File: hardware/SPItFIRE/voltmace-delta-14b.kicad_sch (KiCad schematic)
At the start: 17 parts, among them J2 DA15_Pins, SW10 SW_Push_45deg, SW10L1 SW_Push_45deg, SW10M1 SW_Push_45deg, SW10R1 SW_Push_45deg, SW12 SW_Push_45deg, SW13 SW_Push_45deg, SW14 SW_Push_45deg, SW15 SW_Push_45deg, SW16 SW_Push_45deg, SW17 SW_Push_45deg, SW18 SW_Push_45deg, SW19 SW_Push_45deg, SW20 SW_Push_45deg, SW21 SW_Push_45deg

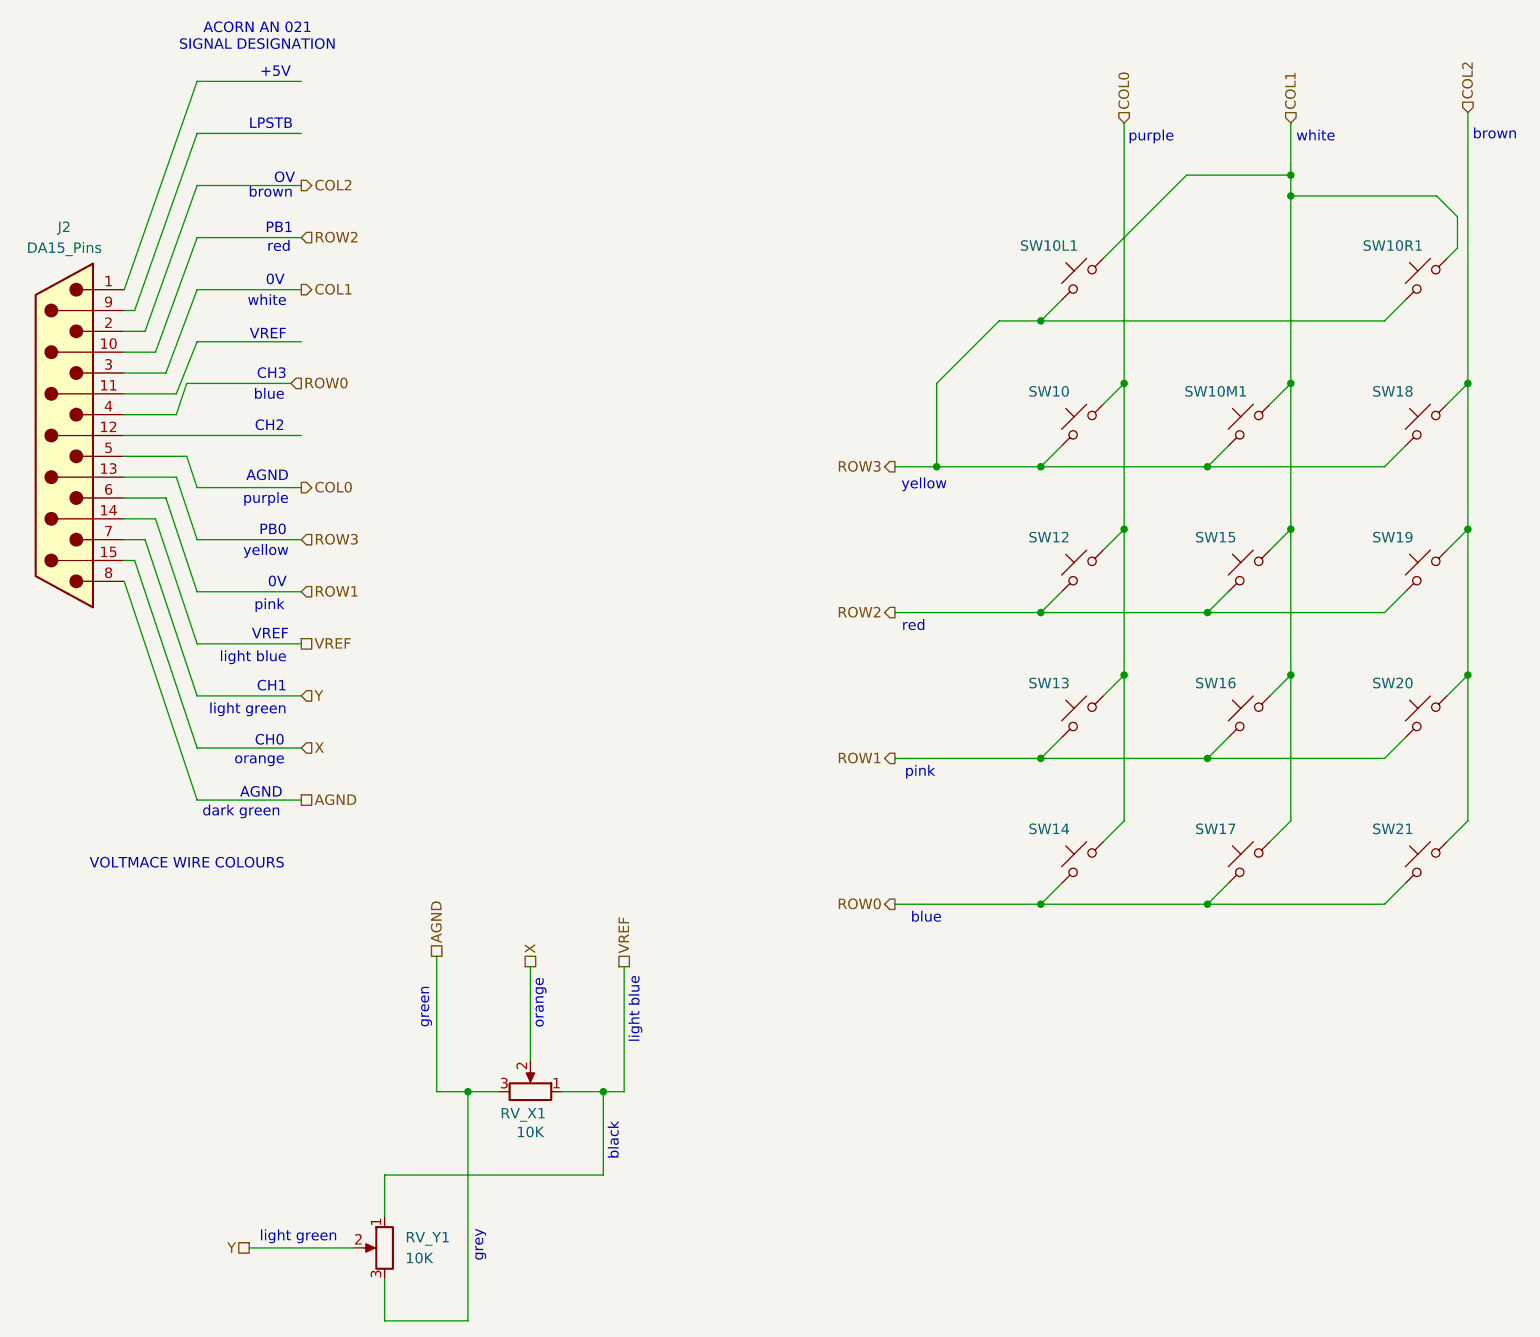
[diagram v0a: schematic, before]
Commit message: Voltmace pinouts
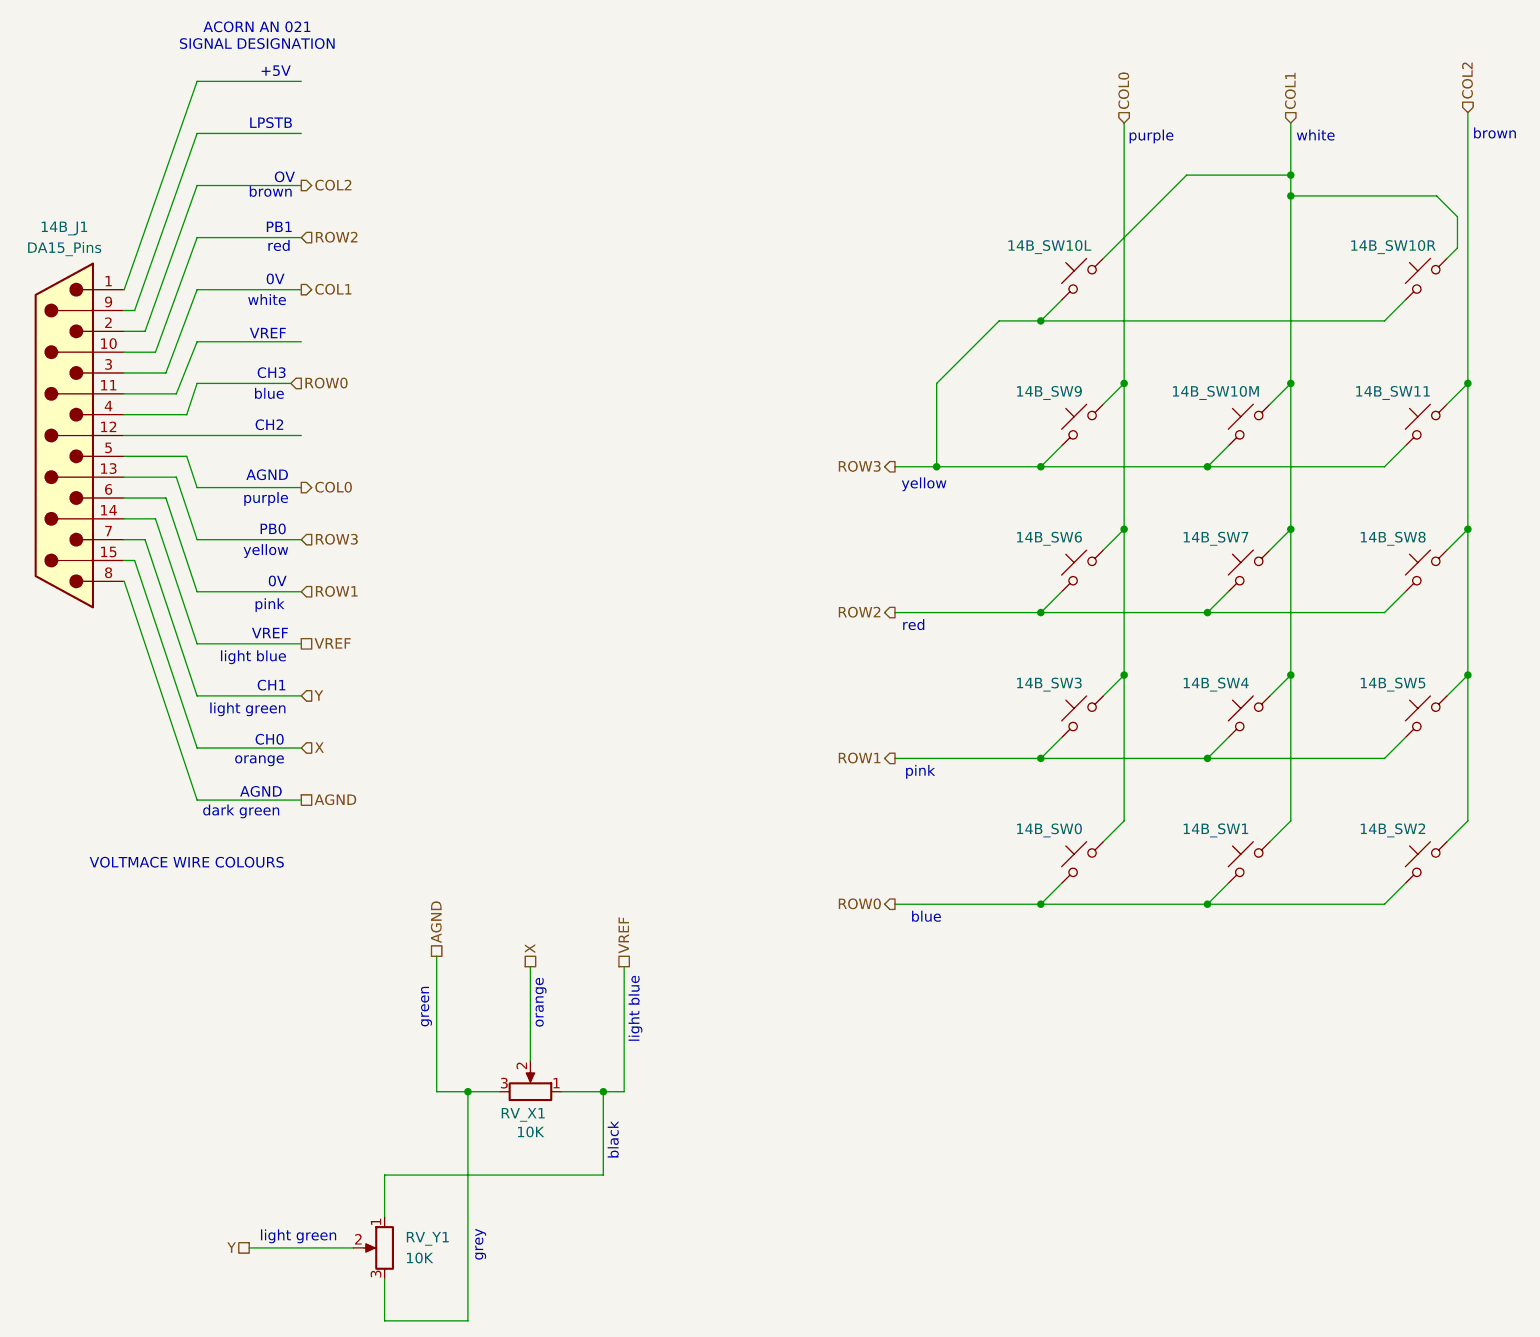
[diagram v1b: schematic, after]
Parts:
- renumbered J2 to 14B_J1, SW14 to 14B_SW0, SW17 to 14B_SW1, SW10L1 to 14B_SW10L, SW10M1 to 14B_SW10M, SW10R1 to 14B_SW10R, SW18 to 14B_SW11, SW21 to 14B_SW2, SW13 to 14B_SW3, SW16 to 14B_SW4, SW20 to 14B_SW5, SW12 to 14B_SW6, SW15 to 14B_SW7, SW19 to 14B_SW8, SW10 to 14B_SW9
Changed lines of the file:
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@@
 	(wire
 		(pts
-			(xy 71.12 69.85) (xy 72.39 66.04)
+			(xy 72.39 69.85) (xy 73.66 66.04)
 		)
 		(stroke
@@
 	(wire
 		(pts
-			(xy 72.39 66.04) (xy 85.09 66.04)
+			(xy 73.66 66.04) (xy 85.09 66.04)
 		)
 		(stroke
@@
 	(wire
 		(pts
-			(xy 64.77 69.85) (xy 71.12 69.85)
+			(xy 64.77 69.85) (xy 72.39 69.85)
 		)
 		(stroke
@@
 		(on_board yes)
 		(dnp no)
-		(property "Reference" "SW20"
+		(property "Reference" "14B_SW5"
 			(at 219.456 102.616 0)
 			(effects
@@
 			(project "SPItFIRE"
 				(path "/148e0ceb-efca-48fe-9d35-9803ba402dc8/b2803d4d-10bd-4088-a3d9-c185506ad2c5"
-					(reference "SW20")
+					(reference "14B_SW5")
 					(unit 1)
 				)
@@
 		(on_board yes)
 		(dnp no)
-		(property "Reference" "SW10L1"
+		(property "Reference" "14B_SW10L"
 			(at 177.546 49.276 0)
 			(effects
@@
 			(project "SPItFIRE"
 				(path "/148e0ceb-efca-48fe-9d35-9803ba402dc8/b2803d4d-10bd-4088-a3d9-c185506ad2c5"
-					(reference "SW10L1")
+					(reference "14B_SW10L")
 					(unit 1)
 				)
@@
 		(on_board yes)
 		(dnp no)
-		(property "Reference" "SW13"
+		(property "Reference" "14B_SW3"
 			(at 177.546 102.616 0)
 			(effects
@@
 			(project "SPItFIRE"
 				(path "/148e0ceb-efca-48fe-9d35-9803ba402dc8/b2803d4d-10bd-4088-a3d9-c185506ad2c5"
-					(reference "SW13")
+					(reference "14B_SW3")
 					(unit 1)
 				)
@@
 		(on_board yes)
 		(dnp no)
-		(property "Reference" "SW21"
+		(property "Reference" "14B_SW2"
 			(at 219.456 120.396 0)
 			(effects
@@
 			(project "SPItFIRE"
 				(path "/148e0ceb-efca-48fe-9d35-9803ba402dc8/b2803d4d-10bd-4088-a3d9-c185506ad2c5"
-					(reference "SW21")
+					(reference "14B_SW2")
 					(unit 1)
 				)
@@
 		(on_board yes)
 		(dnp no)
-		(property "Reference" "SW12"
+		(property "Reference" "14B_SW6"
 			(at 177.546 84.836 0)
 			(effects
@@
 			(project "SPItFIRE"
 				(path "/148e0ceb-efca-48fe-9d35-9803ba402dc8/b2803d4d-10bd-4088-a3d9-c185506ad2c5"
-					(reference "SW12")
+					(reference "14B_SW6")
 					(unit 1)
 				)
@@
 		(on_board yes)
 		(dnp no)
-		(property "Reference" "SW18"
+		(property "Reference" "14B_SW11"
 			(at 219.456 67.056 0)
 			(effects
@@
 			(project "SPItFIRE"
 				(path "/148e0ceb-efca-48fe-9d35-9803ba402dc8/b2803d4d-10bd-4088-a3d9-c185506ad2c5"
-					(reference "SW18")
+					(reference "14B_SW11")
 					(unit 1)
 				)
@@
 		(on_board yes)
 		(dnp no)
-		(property "Reference" "SW10M1"
+		(property "Reference" "14B_SW10M"
 			(at 197.866 67.056 0)
 			(effects
@@
 			(project "SPItFIRE"
 				(path "/148e0ceb-efca-48fe-9d35-9803ba402dc8/b2803d4d-10bd-4088-a3d9-c185506ad2c5"
-					(reference "SW10M1")
+					(reference "14B_SW10M")
 					(unit 1)
 				)
@@
 		(on_board yes)
 		(dnp no)
-		(property "Reference" "SW10"
+		(property "Reference" "14B_SW9"
 			(at 177.546 67.056 0)
 			(effects
@@
 			(project "SPItFIRE"
 				(path "/148e0ceb-efca-48fe-9d35-9803ba402dc8/b2803d4d-10bd-4088-a3d9-c185506ad2c5"
-					(reference "SW10")
+					(reference "14B_SW9")
 					(unit 1)
 				)
@@
 		(on_board yes)
 		(dnp no)
-		(property "Reference" "SW10R1"
+		(property "Reference" "14B_SW10R"
 			(at 219.456 49.276 0)
 			(effects
@@
 			(project "SPItFIRE"
 				(path "/148e0ceb-efca-48fe-9d35-9803ba402dc8/b2803d4d-10bd-4088-a3d9-c185506ad2c5"
-					(reference "SW10R1")
+					(reference "14B_SW10R")
 					(unit 1)
 				)
@@
 		(on_board yes)
 		(dnp no)
-		(property "Reference" "SW14"
+		(property "Reference" "14B_SW0"
 			(at 177.546 120.396 0)
 			(effects
@@
 			(project "SPItFIRE"
 				(path "/148e0ceb-efca-48fe-9d35-9803ba402dc8/b2803d4d-10bd-4088-a3d9-c185506ad2c5"
-					(reference "SW14")
+					(reference "14B_SW0")
 					(unit 1)
 				)
@@
 		(on_board yes)
 		(dnp no)
-		(property "Reference" "SW17"
+		(property "Reference" "14B_SW1"
 			(at 197.866 120.396 0)
 			(effects
@@
 			(project "SPItFIRE"
 				(path "/148e0ceb-efca-48fe-9d35-9803ba402dc8/b2803d4d-10bd-4088-a3d9-c185506ad2c5"
-					(reference "SW17")
+					(reference "14B_SW1")
 					(unit 1)
 				)
@@
 		(on_board yes)
 		(dnp no)
-		(property "Reference" "SW15"
+		(property "Reference" "14B_SW7"
 			(at 197.866 84.836 0)
 			(effects
@@
 			(project "SPItFIRE"
 				(path "/148e0ceb-efca-48fe-9d35-9803ba402dc8/b2803d4d-10bd-4088-a3d9-c185506ad2c5"
-					(reference "SW15")
+					(reference "14B_SW7")
 					(unit 1)
 				)
@@
 		(on_board yes)
 		(dnp no)
-		(property "Reference" "SW19"
+		(property "Reference" "14B_SW8"
 			(at 219.456 84.836 0)
 			(effects
@@
 			(project "SPItFIRE"
 				(path "/148e0ceb-efca-48fe-9d35-9803ba402dc8/b2803d4d-10bd-4088-a3d9-c185506ad2c5"
-					(reference "SW19")
+					(reference "14B_SW8")
 					(unit 1)
 				)
@@
 		(dnp no)
 		(fields_autoplaced yes)
-		(property "Reference" "J2"
+		(property "Reference" "14B_J1"
 			(at 57.4675 46.99 0)
 			(effects
@@
 			(project "SPItFIRE"
 				(path "/148e0ceb-efca-48fe-9d35-9803ba402dc8/b2803d4d-10bd-4088-a3d9-c185506ad2c5"
-					(reference "J2")
+					(reference "14B_J1")
 					(unit 1)
 				)
@@
 		(on_board yes)
 		(dnp no)
-		(property "Reference" "SW16"
+		(property "Reference" "14B_SW4"
 			(at 197.866 102.616 0)
 			(effects
@@
 			(project "SPItFIRE"
 				(path "/148e0ceb-efca-48fe-9d35-9803ba402dc8/b2803d4d-10bd-4088-a3d9-c185506ad2c5"
-					(reference "SW16")
+					(reference "14B_SW4")
 					(unit 1)
 				)

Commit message: Update schematic naming convention to keep Kicad happy
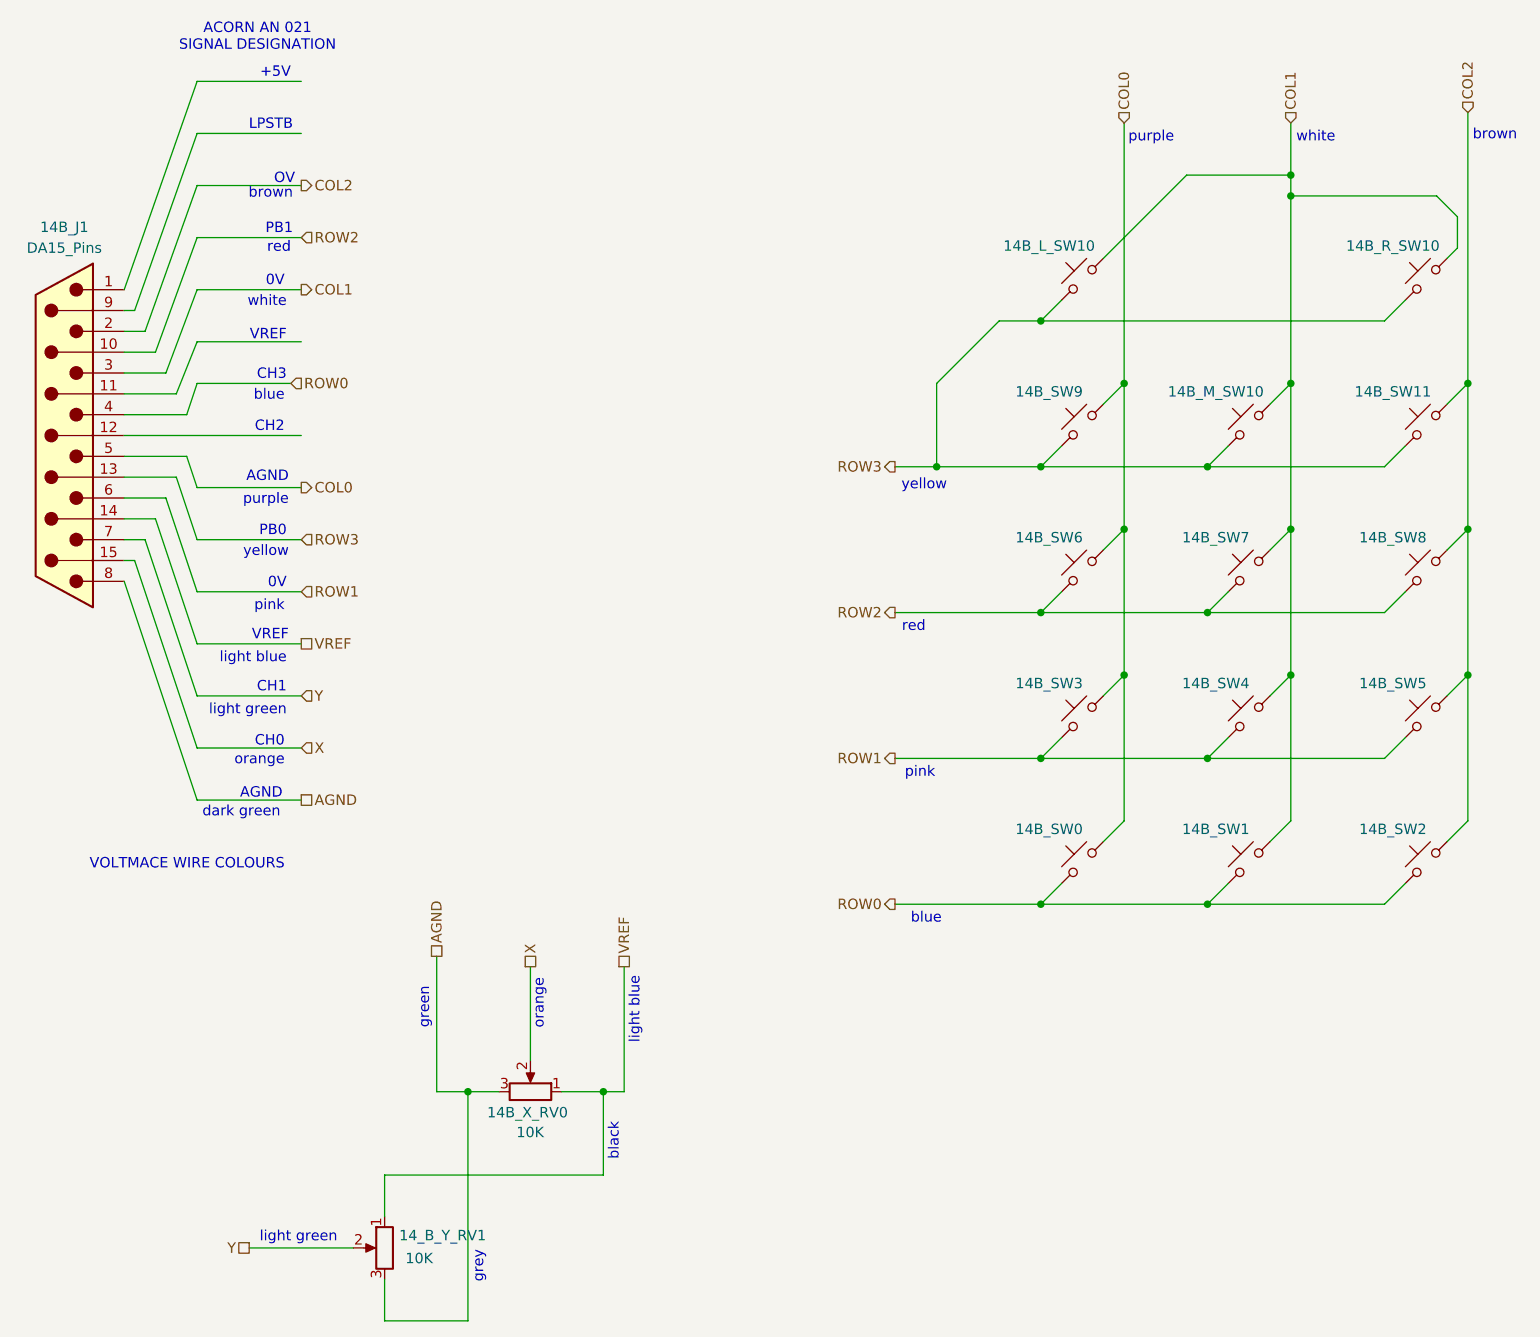
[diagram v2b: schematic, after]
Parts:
- renumbered 14B_SW10L to 14B_L_SW10, 14B_SW10M to 14B_M_SW10, 14B_SW10R to 14B_R_SW10, RV_X1 to 14B_X_RV0, RV_Y1 to 14_B_Y_RV1
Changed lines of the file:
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@@
 	(text "grey"
 		(exclude_from_sim no)
-		(at 107.95 173.228 90)
+		(at 107.95 175.768 90)
 		(effects
 			(font
@@
 				)
 			)
+			(project "voltmace-delta-14b"
+				(path "/e608229c-3d92-4eb5-a64c-33adb7986997"
+					(reference "14B_SW5")
+					(unit 1)
+				)
+			)
 		)
 	)
@@
 		(on_board yes)
 		(dnp no)
-		(property "Reference" "14B_SW10L"
+		(property "Reference" "14B_L_SW10"
 			(at 177.546 49.276 0)
 			(effects
@@
 				(path "/148e0ceb-efca-48fe-9d35-9803ba402dc8/b2803d4d-10bd-4088-a3d9-c185506ad2c5"
 					(reference "14B_SW10L")
+					(unit 1)
+				)
+			)
+			(project "voltmace-delta-14b"
+				(path "/e608229c-3d92-4eb5-a64c-33adb7986997"
+					(reference "14B_L_SW10")
 					(unit 1)
 				)
@@
 				)
 			)
+			(project "voltmace-delta-14b"
+				(path "/e608229c-3d92-4eb5-a64c-33adb7986997"
+					(reference "14B_SW3")
+					(unit 1)
+				)
+			)
 		)
 	)
@@
 				)
 			)
+			(project "voltmace-delta-14b"
+				(path "/e608229c-3d92-4eb5-a64c-33adb7986997"
+					(reference "14B_SW2")
+					(unit 1)
+				)
+			)
 		)
 	)
@@
 				)
 			)
+			(project "voltmace-delta-14b"
+				(path "/e608229c-3d92-4eb5-a64c-33adb7986997"
+					(reference "14B_SW6")
+					(unit 1)
+				)
+			)
 		)
 	)
@@
 				)
 			)
+			(project "voltmace-delta-14b"
+				(path "/e608229c-3d92-4eb5-a64c-33adb7986997"
+					(reference "14B_SW11")
+					(unit 1)
+				)
+			)
 		)
 	)
@@
 		(on_board yes)
 		(dnp no)
-		(property "Reference" "14B_SW10M"
+		(property "Reference" "14B_M_SW10"
 			(at 197.866 67.056 0)
 			(effects
@@
 				(path "/148e0ceb-efca-48fe-9d35-9803ba402dc8/b2803d4d-10bd-4088-a3d9-c185506ad2c5"
 					(reference "14B_SW10M")
+					(unit 1)
+				)
+			)
+			(project "voltmace-delta-14b"
+				(path "/e608229c-3d92-4eb5-a64c-33adb7986997"
+					(reference "14B_M_SW10")
 					(unit 1)
 				)
@@
 				)
 			)
+			(project "voltmace-delta-14b"
+				(path "/e608229c-3d92-4eb5-a64c-33adb7986997"
+					(reference "14B_SW9")
+					(unit 1)
+				)
+			)
 		)
 	)
@@
 		(on_board yes)
 		(dnp no)
-		(fields_autoplaced yes)
-		(property "Reference" "RV_Y1"
-			(at 99.06 170.1799 0)
+		(property "Reference" "14_B_Y_RV1"
+			(at 98.298 169.926 0)
 			(effects
 				(font
@@
 				(path "/148e0ceb-efca-48fe-9d35-9803ba402dc8/b2803d4d-10bd-4088-a3d9-c185506ad2c5"
 					(reference "RV_Y1")
+					(unit 1)
+				)
+			)
+			(project "voltmace-delta-14b"
+				(path "/e608229c-3d92-4eb5-a64c-33adb7986997"
+					(reference "14_B_Y_RV1")
 					(unit 1)
 				)
@@
 		(on_board yes)
 		(dnp no)
-		(property "Reference" "14B_SW10R"
+		(property "Reference" "14B_R_SW10"
 			(at 219.456 49.276 0)
 			(effects
@@
 				(path "/148e0ceb-efca-48fe-9d35-9803ba402dc8/b2803d4d-10bd-4088-a3d9-c185506ad2c5"
 					(reference "14B_SW10R")
+					(unit 1)
+				)
+			)
+			(project "voltmace-delta-14b"
+				(path "/e608229c-3d92-4eb5-a64c-33adb7986997"
+					(reference "14B_R_SW10")
 					(unit 1)
 				)
@@
 				)
 			)
+			(project "voltmace-delta-14b"
+				(path "/e608229c-3d92-4eb5-a64c-33adb7986997"
+					(reference "14B_SW0")
+					(unit 1)
+				)
+			)
 		)
 	)
@@
 				)
 			)
+			(project "voltmace-delta-14b"
+				(path "/e608229c-3d92-4eb5-a64c-33adb7986997"
+					(reference "14B_SW1")
+					(unit 1)
+				)
+			)
 		)
 	)
@@
 				)
 			)
+			(project "voltmace-delta-14b"
+				(path "/e608229c-3d92-4eb5-a64c-33adb7986997"
+					(reference "14B_SW7")
+					(unit 1)
+				)
+			)
 		)
 	)
@@
 				)
 			)
+			(project "voltmace-delta-14b"
+				(path "/e608229c-3d92-4eb5-a64c-33adb7986997"
+					(reference "14B_SW8")
+					(unit 1)
+				)
+			)
 		)
 	)
@@
 				)
 			)
+			(project "voltmace-delta-14b"
+				(path "/e608229c-3d92-4eb5-a64c-33adb7986997"
+					(reference "14B_J1")
+					(unit 1)
+				)
+			)
 		)
 	)
@@
 		(on_board yes)
 		(dnp no)
-		(property "Reference" "RV_X1"
-			(at 116.205 155.067 90)
+		(property "Reference" "14B_X_RV0"
+			(at 118.872 154.94 90)
 			(effects
 				(font
@@
 				(path "/148e0ceb-efca-48fe-9d35-9803ba402dc8/b2803d4d-10bd-4088-a3d9-c185506ad2c5"
 					(reference "RV_X1")
+					(unit 1)
+				)
+			)
+			(project "voltmace-delta-14b"
+				(path "/e608229c-3d92-4eb5-a64c-33adb7986997"
+					(reference "14B_X_RV0")
 					(unit 1)
 				)
@@
 				)
 			)
-		)
-	)
+			(project "voltmace-delta-14b"
+				(path "/e608229c-3d92-4eb5-a64c-33adb7986997"
+					(reference "14B_SW4")
+					(unit 1)
+				)
+			)
+		)
+	)
+	(sheet_instances
+		(path "/"
+			(page "1")
+		)
+	)
+	(embedded_fonts no)
 )
